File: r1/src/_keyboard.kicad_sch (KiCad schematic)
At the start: 36 parts, among them SW1 REV_TACT, SW10 REV_TACT, SW11 REV_TACT, SW12 REV_TACT, SW13 REV_TACT, SW14 REV_TACT, SW15 REV_TACT, SW16 REV_TACT, SW17 REV_TACT, SW18 REV_TACT, SW19 REV_TACT, SW2 REV_TACT, SW20 REV_TACT, SW21 REV_TACT, SW22 REV_TACT, SW23 REV_TACT, SW24 REV_TACT, SW25 REV_TACT, SW26 REV_TACT, SW27 REV_TACT, SW28 REV_TACT, SW29 REV_TACT, SW3 REV_TACT, SW30 REV_TACT, SW31 REV_TACT, SW32 REV_TACT, SW4 REV_TACT, SW5 REV_TACT, SW6 REV_TACT, SW7 REV_TACT, SW8 REV_TACT, SW9 REV_TACT, U10 PCA9555, U6 PCA9555

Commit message: Assign MPN's and LCSC part numbers
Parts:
- U10, U6: value PCA9555 -> PCA9555PW; LCSC (none) -> C128392; MPN (none) -> PCA9555PW
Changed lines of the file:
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@@
       (effects (font (size 1.27 1.27)) (justify left))
     )
-    (property "Value" "PCA9555" (at 74.3459 114.3 0)
+    (property "Value" "PCA9555PW" (at 74.3459 114.3 0)
       (effects (font (size 1.27 1.27)) (justify left))
     )
@@
     )
     (property "Datasheet" "" (at 72.39 137.16 0)
+      (effects (font (size 1.27 1.27)) hide)
+    )
+    (property "MPN" "PCA9555PW" (at 72.39 137.16 0)
+      (effects (font (size 1.27 1.27)) hide)
+    )
+    (property "LCSC" "C128392" (at 72.39 137.16 0)
       (effects (font (size 1.27 1.27)) hide)
     )
@@
       (effects (font (size 1.27 1.27)) (justify left))
     )
-    (property "Value" "PCA9555" (at 74.3459 40.64 0)
+    (property "Value" "PCA9555PW" (at 74.3459 40.64 0)
       (effects (font (size 1.27 1.27)) (justify left))
     )
@@
       (effects (font (size 1.27 1.27)) hide)
     )
+    (property "MPN" "PCA9555PW" (at 72.39 63.5 0)
+      (effects (font (size 1.27 1.27)) hide)
+    )
+    (property "LCSC" "C128392" (at 72.39 63.5 0)
+      (effects (font (size 1.27 1.27)) hide)
+    )

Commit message: Assign manufacturers
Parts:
- U10, U6: Manufacturer (none) -> Texas Instruments
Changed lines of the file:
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@@
+      (effects (font (size 1.27 1.27)) hide)
+    )
+    (property "Manufacturer" "Texas Instruments" (at 72.39 137.16 0)
       (effects (font (size 1.27 1.27)) hide)
     )
@@
       (effects (font (size 1.27 1.27)) hide)
     )
+    (property "Manufacturer" "Texas Instruments" (at 72.39 63.5 0)
+      (effects (font (size 1.27 1.27)) hide)
+    )

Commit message: Reannotate component refs
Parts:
- renumbered SW11 to SW10, SW21 to SW11, SW22 to SW12, SW4 to SW13, SW12 to SW14, SW23 to SW15, SW24 to SW16, SW5 to SW17, SW13 to SW18, SW25 to SW19, SW9 to SW2, SW26 to SW20, SW6 to SW21, SW14 to SW22, SW27 to SW23, SW28 to SW24, SW7 to SW25, SW15 to SW26, SW29 to SW27, SW30 to SW28, SW8 to SW29, SW17 to SW3, SW16 to SW30, SW18 to SW4, SW2 to SW5, SW10 to SW6, SW19 to SW7, SW20 to SW8, SW3 to SW9, U6 to U7, U10 to U8

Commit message: Assign footprints from jeffmakes-footprints lib
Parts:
- SW1: footprint (none) -> jeffmakes_footprints:microSD_HC_Sofng_TF-15
- U7: footprint (none) -> jeffmakes_footprints:SW_JS1400BFQ-arrows
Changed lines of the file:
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@@
       (effects (font (size 1.27 1.27)) (justify left))
     )
-    (property "Footprint" "" (at 72.39 63.5 0)
+    (property "Footprint" "jeffmakes_footprints:SW_JS1400BFQ-arrows" (at 72.39 63.5 0)
       (effects (font (size 1.27 1.27)) hide)
     )
@@
       (effects (font (size 1.27 1.27)) (justify right))
     )
-    (property "Footprint" "" (at 133.35 52.07 0)
-      (effects (font (size 1.27 1.27)) hide)
-    )
+    (property "Footprint" "jeffmakes_footprints:microSD_HC_Sofng_TF-15" (at 133.35 52.07 0)
+      (effects (font (size 1.27 1.27)) hide)
+    )

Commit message: Assign footprints
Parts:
- SW1: footprint jeffmakes_footprints:microSD_HC_Sofng_TF-15 -> (none)
- U7: footprint jeffmakes_footprints:SW_JS1400BFQ-arrows -> Package_SO:TSSOP-24_4.4x7.8mm_P0.65mm
- U8: footprint (none) -> Package_SO:TSSOP-24_4.4x7.8mm_P0.65mm
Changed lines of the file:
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@@
       (effects (font (size 1.27 1.27)) (justify left))
     )
-    (property "Footprint" "" (at 72.39 137.16 0)
+    (property "Footprint" "Package_SO:TSSOP-24_4.4x7.8mm_P0.65mm" (at 72.39 137.16 0)
       (effects (font (size 1.27 1.27)) hide)
     )
@@
       (effects (font (size 1.27 1.27)) (justify left))
     )
-    (property "Footprint" "jeffmakes_footprints:SW_JS1400BFQ-arrows" (at 72.39 63.5 0)
+    (property "Footprint" "Package_SO:TSSOP-24_4.4x7.8mm_P0.65mm" (at 72.39 63.5 0)
       (effects (font (size 1.27 1.27)) hide)
     )
@@
       (effects (font (size 1.27 1.27)) (justify right))
     )
-    (property "Footprint" "jeffmakes_footprints:microSD_HC_Sofng_TF-15" (at 133.35 52.07 0)
-      (effects (font (size 1.27 1.27)) hide)
-    )
+    (property "Footprint" "" (at 133.35 52.07 0)
+      (effects (font (size 1.27 1.27)) hide)
+    )

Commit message: Assign footprints
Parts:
- SW1, SW10, SW11, SW12, SW13, SW14, SW15, SW16, SW17, SW18, SW19, SW2, SW20, SW21, SW22, SW23, SW24, SW25, SW26, SW27, SW28, SW29, SW3, SW30, SW31, SW32, SW4, SW5, SW6, SW7, SW8, SW9: footprint (none) -> jeffmakes_footprints:SW_SPST_TACT_6x6_REV_MOUNT
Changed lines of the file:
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@@
       (effects (font (size 1.27 1.27)) (justify right))
     )
-    (property "Footprint" "" (at 240.03 77.47 0)
+    (property "Footprint" "jeffmakes_footprints:SW_SPST_TACT_6x6_REV_MOUNT" (at 240.03 77.47 0)
       (effects (font (size 1.27 1.27)) hide)
     )
@@
       (effects (font (size 1.27 1.27)) (justify right))
     )
-    (property "Footprint" "" (at 163.83 128.27 0)
+    (property "Footprint" "jeffmakes_footprints:SW_SPST_TACT_6x6_REV_MOUNT" (at 163.83 128.27 0)
       (effects (font (size 1.27 1.27)) hide)
     )
@@
       (effects (font (size 1.27 1.27)) (justify right))
     )
-    (property "Footprint" "" (at 194.31 128.27 0)
+    (property "Footprint" "jeffmakes_footprints:SW_SPST_TACT_6x6_REV_MOUNT" (at 194.31 128.27 0)
       (effects (font (size 1.27 1.27)) hide)
     )
@@
       (effects (font (size 1.27 1.27)) (justify right))
     )
-    (property "Footprint" "" (at 133.35 102.87 0)
+    (property "Footprint" "jeffmakes_footprints:SW_SPST_TACT_6x6_REV_MOUNT" (at 133.35 102.87 0)
       (effects (font (size 1.27 1.27)) hide)
     )
@@
       (effects (font (size 1.27 1.27)) (justify right))
     )
-    (property "Footprint" "" (at 224.79 102.87 0)
+    (property "Footprint" "jeffmakes_footprints:SW_SPST_TACT_6x6_REV_MOUNT" (at 224.79 102.87 0)
       (effects (font (size 1.27 1.27)) hide)
     )
@@
       (effects (font (size 1.27 1.27)) (justify right))
     )
-    (property "Footprint" "" (at 240.03 128.27 0)
+    (property "Footprint" "jeffmakes_footprints:SW_SPST_TACT_6x6_REV_MOUNT" (at 240.03 128.27 0)
       (effects (font (size 1.27 1.27)) hide)
     )
@@
       (effects (font (size 1.27 1.27)) (justify right))
     )
-    (property "Footprint" "" (at 179.07 77.47 0)
+    (property "Footprint" "jeffmakes_footprints:SW_SPST_TACT_6x6_REV_MOUNT" (at 179.07 77.47 0)
       (effects (font (size 1.27 1.27)) hide)
     )
@@
       (effects (font (size 1.27 1.27)) (justify right))
     )
-    (property "Footprint" "" (at 179.07 52.07 0)
+    (property "Footprint" "jeffmakes_footprints:SW_SPST_TACT_6x6_REV_MOUNT" (at 179.07 52.07 0)
       (effects (font (size 1.27 1.27)) hide)
     )
@@
       (effects (font (size 1.27 1.27)) (justify right))
     )
-    (property "Footprint" "" (at 209.55 102.87 0)
+    (property "Footprint" "jeffmakes_footprints:SW_SPST_TACT_6x6_REV_MOUNT" (at 209.55 102.87 0)
       (effects (font (size 1.27 1.27)) hide)
     )
@@
       (effects (font (size 1.27 1.27)) (justify right))
     )
-    (property "Footprint" "" (at 209.55 77.47 0)
+    (property "Footprint" "jeffmakes_footprints:SW_SPST_TACT_6x6_REV_MOUNT" (at 209.55 77.47 0)
       (effects (font (size 1.27 1.27)) hide)
     )
@@
       (effects (font (size 1.27 1.27)) (justify right))
     )
-    (property "Footprint" "" (at 179.07 102.87 0)
+    (property "Footprint" "jeffmakes_footprints:SW_SPST_TACT_6x6_REV_MOUNT" (at 179.07 102.87 0)
       (effects (font (size 1.27 1.27)) hide)
     )
@@
       (effects (font (size 1.27 1.27)) (justify right))
     )
-    (property "Footprint" "" (at 240.03 52.07 0)
+    (property "Footprint" "jeffmakes_footprints:SW_SPST_TACT_6x6_REV_MOUNT" (at 240.03 52.07 0)
       (effects (font (size 1.27 1.27)) hide)
     )
@@
       (effects (font (size 1.27 1.27)) (justify right))
     )
-    (property "Footprint" "" (at 148.59 77.47 0)
+    (property "Footprint" "jeffmakes_footprints:SW_SPST_TACT_6x6_REV_MOUNT" (at 148.59 77.47 0)
       (effects (font (size 1.27 1.27)) hide)
     )
@@
       (effects (font (size 1.27 1.27)) (justify right))
     )
-    (property "Footprint" "" (at 240.03 102.87 0)
+    (property "Footprint" "jeffmakes_footprints:SW_SPST_TACT_6x6_REV_MOUNT" (at 240.03 102.87 0)
       (effects (font (size 1.27 1.27)) hide)
     )
@@
       (effects (font (size 1.27 1.27)) (justify right))
     )
-    (property "Footprint" "" (at 209.55 128.27 0)
+    (property "Footprint" "jeffmakes_footprints:SW_SPST_TACT_6x6_REV_MOUNT" (at 209.55 128.27 0)
       (effects (font (size 1.27 1.27)) hide)
     )
@@
       (effects (font (size 1.27 1.27)) (justify right))
     )
-    (property "Footprint" "" (at 133.35 77.47 0)
+    (property "Footprint" "jeffmakes_footprints:SW_SPST_TACT_6x6_REV_MOUNT" (at 133.35 77.47 0)
       (effects (font (size 1.27 1.27)) hide)
     )
@@
       (effects (font (size 1.27 1.27)) (justify right))
     )
-    (property "Footprint" "" (at 224.79 77.47 0)
+    (property "Footprint" "jeffmakes_footprints:SW_SPST_TACT_6x6_REV_MOUNT" (at 224.79 77.47 0)
       (effects (font (size 1.27 1.27)) hide)
     )
@@
       (effects (font (size 1.27 1.27)) (justify right))
     )
-    (property "Footprint" "" (at 148.59 52.07 0)
+    (property "Footprint" "jeffmakes_footprints:SW_SPST_TACT_6x6_REV_MOUNT" (at 148.59 52.07 0)
       (effects (font (size 1.27 1.27)) hide)
     )
@@
       (effects (font (size 1.27 1.27)) (justify right))
     )
-    (property "Footprint" "" (at 133.35 52.07 0)
+    (property "Footprint" "jeffmakes_footprints:SW_SPST_TACT_6x6_REV_MOUNT" (at 133.35 52.07 0)
       (effects (font (size 1.27 1.27)) hide)
     )
@@
       (effects (font (size 1.27 1.27)) (justify right))
     )
-    (property "Footprint" "" (at 163.83 77.47 0)
+    (property "Footprint" "jeffmakes_footprints:SW_SPST_TACT_6x6_REV_MOUNT" (at 163.83 77.47 0)
       (effects (font (size 1.27 1.27)) hide)
     )
@@
       (effects (font (size 1.27 1.27)) (justify right))
     )
-    (property "Footprint" "" (at 224.79 128.27 0)
+    (property "Footprint" "jeffmakes_footprints:SW_SPST_TACT_6x6_REV_MOUNT" (at 224.79 128.27 0)
       (effects (font (size 1.27 1.27)) hide)
     )
@@
       (effects (font (size 1.27 1.27)) (justify right))
     )
-    (property "Footprint" "" (at 179.07 128.27 0)
+    (property "Footprint" "jeffmakes_footprints:SW_SPST_TACT_6x6_REV_MOUNT" (at 179.07 128.27 0)
       (effects (font (size 1.27 1.27)) hide)
     )
@@
       (effects (font (size 1.27 1.27)) (justify right))
     )
-    (property "Footprint" "" (at 163.83 102.87 0)
+    (property "Footprint" "jeffmakes_footprints:SW_SPST_TACT_6x6_REV_MOUNT" (at 163.83 102.87 0)
       (effects (font (size 1.27 1.27)) hide)
     )
@@
       (effects (font (size 1.27 1.27)) (justify right))
     )
-    (property "Footprint" "" (at 133.35 128.27 0)
+    (property "Footprint" "jeffmakes_footprints:SW_SPST_TACT_6x6_REV_MOUNT" (at 133.35 128.27 0)
       (effects (font (size 1.27 1.27)) hide)
     )
@@
       (effects (font (size 1.27 1.27)) (justify right))
     )
-    (property "Footprint" "" (at 209.55 52.07 0)
+    (property "Footprint" "jeffmakes_footprints:SW_SPST_TACT_6x6_REV_MOUNT" (at 209.55 52.07 0)
       (effects (font (size 1.27 1.27)) hide)
     )
@@
       (effects (font (size 1.27 1.27)) (justify right))
     )
-    (property "Footprint" "" (at 148.59 102.87 0)
+    (property "Footprint" "jeffmakes_footprints:SW_SPST_TACT_6x6_REV_MOUNT" (at 148.59 102.87 0)
       (effects (font (size 1.27 1.27)) hide)
     )
@@
       (effects (font (size 1.27 1.27)) (justify right))
     )
-    (property "Footprint" "" (at 194.31 52.07 0)
+    (property "Footprint" "jeffmakes_footprints:SW_SPST_TACT_6x6_REV_MOUNT" (at 194.31 52.07 0)
       (effects (font (size 1.27 1.27)) hide)
     )
@@
       (effects (font (size 1.27 1.27)) (justify right))
     )
-    (property "Footprint" "" (at 148.59 128.27 0)
+    (property "Footprint" "jeffmakes_footprints:SW_SPST_TACT_6x6_REV_MOUNT" (at 148.59 128.27 0)
       (effects (font (size 1.27 1.27)) hide)
     )
@@
       (effects (font (size 1.27 1.27)) (justify right))
     )
-    (property "Footprint" "" (at 224.79 52.07 0)
+    (property "Footprint" "jeffmakes_footprints:SW_SPST_TACT_6x6_REV_MOUNT" (at 224.79 52.07 0)
       (effects (font (size 1.27 1.27)) hide)
     )
@@
       (effects (font (size 1.27 1.27)) (justify right))
     )
-    (property "Footprint" "" (at 194.31 77.47 0)
+    (property "Footprint" "jeffmakes_footprints:SW_SPST_TACT_6x6_REV_MOUNT" (at 194.31 77.47 0)
       (effects (font (size 1.27 1.27)) hide)
     )
@@
       (effects (font (size 1.27 1.27)) (justify right))
     )
-    (property "Footprint" "" (at 163.83 52.07 0)
+    (property "Footprint" "jeffmakes_footprints:SW_SPST_TACT_6x6_REV_MOUNT" (at 163.83 52.07 0)
       (effects (font (size 1.27 1.27)) hide)
     )
@@
       (effects (font (size 1.27 1.27)) (justify right))
     )
-    (property "Footprint" "" (at 194.31 102.87 0)
-      (effects (font (size 1.27 1.27)) hide)
-    )
+    (property "Footprint" "jeffmakes_footprints:SW_SPST_TACT_6x6_REV_MOUNT" (at 194.31 102.87 0)
+      (effects (font (size 1.27 1.27)) hide)
+    )

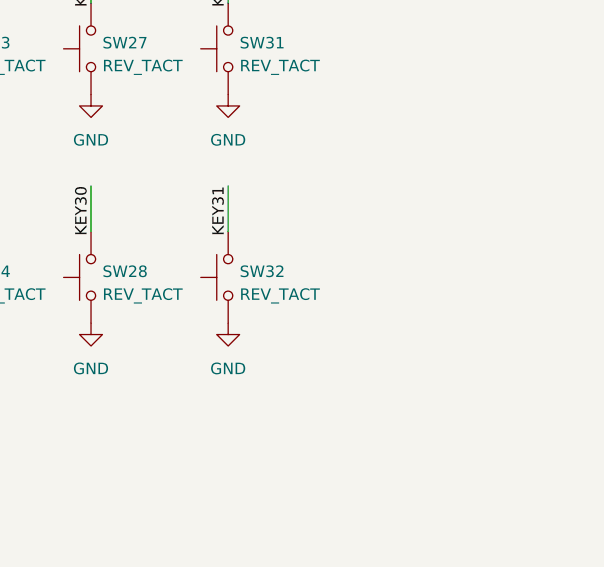
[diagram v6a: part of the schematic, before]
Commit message: ERC pass. Schematic complete.
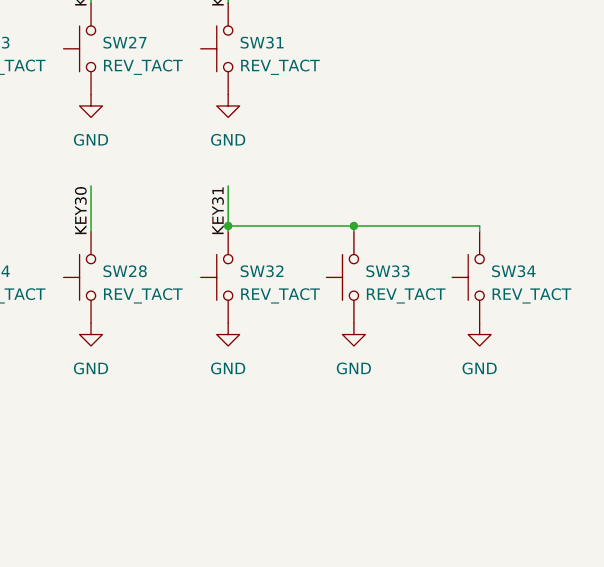
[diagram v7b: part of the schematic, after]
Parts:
- added SW33, SW34: REV_TACT, jeffmakes-footprints:SW_SPST_TACT_6x6_REV_MOUNT, symbol Switch:SW_MEC_5G
- SW1, SW10, SW11, SW12, SW13, SW14, SW15, SW16, SW17, SW18, SW19, SW2, SW20, SW21, SW22, SW23, SW24, SW25, SW26, SW27, SW28, SW29, SW3, SW30, SW31, SW32, SW4, SW5, SW6, SW7, SW8, SW9: footprint jeffmakes_footprints:SW_SPST_TACT_6x6_REV_MOUNT -> jeffmakes-footprints:SW_SPST_TACT_6x6_REV_MOUNT
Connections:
- net GND: now also SW33.1 (A), SW33.2 (A), SW34.1 (A), SW34.2 (A)
- net KEY31: now also SW33.3 (B), SW33.4 (B), SW34.3 (B), SW34.4 (B)

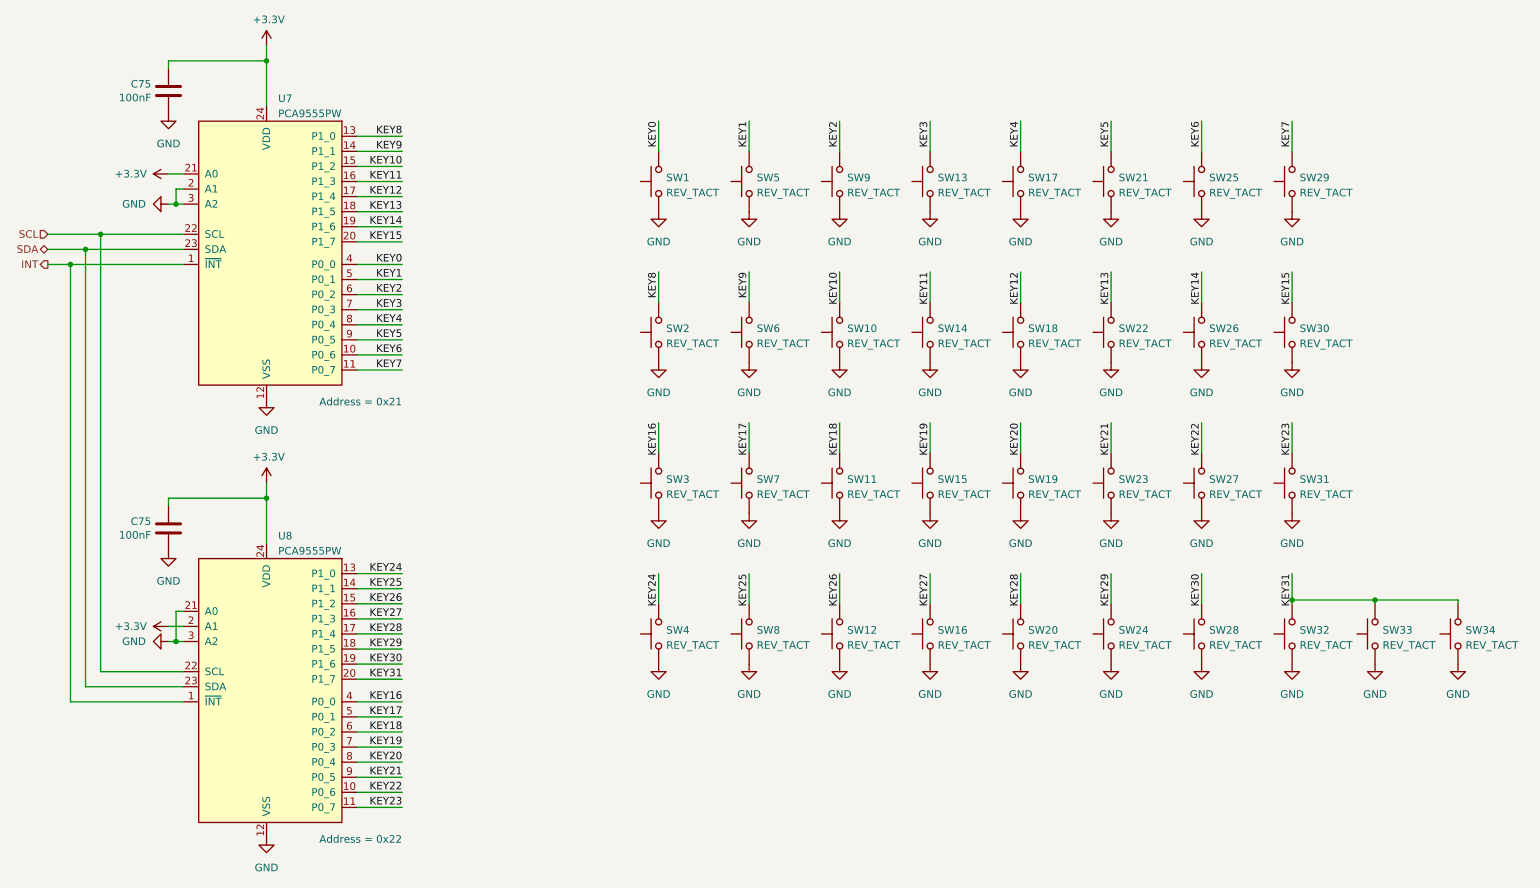
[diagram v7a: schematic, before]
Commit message: Remove duplicate connections from keyboard switches
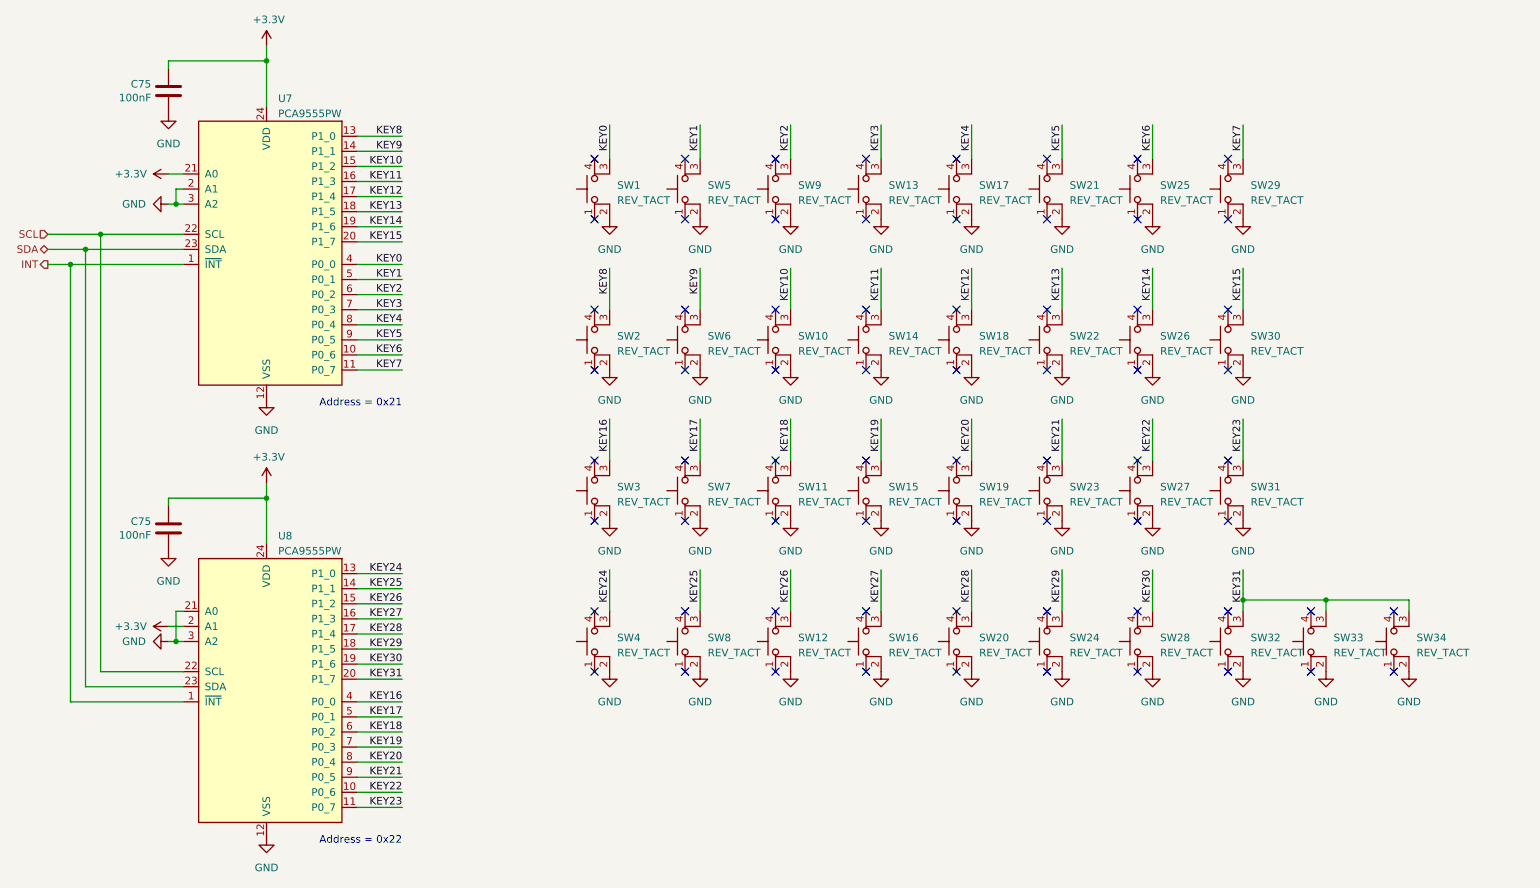
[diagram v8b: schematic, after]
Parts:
- SW1, SW10, SW11, SW12, SW13, SW14, SW15, SW16, SW17, SW18, SW19, SW2, SW20, SW21, SW22, SW23, SW24, SW25, SW26, SW27, SW28, SW29, SW3, SW30, SW31, SW32, SW33, SW34, SW4, SW5, SW6, SW7, SW8, SW9: symbol Switch:SW_MEC_5G -> Switch:SW_MEC_5E
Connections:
- net GND: no longer SW1.1 (A), SW10.1 (A), SW11.1 (A), SW12.1 (A), SW13.1 (A), SW14.1 (A), SW15.1 (A), SW16.1 (A), SW17.1 (A), SW18.1 (A), SW19.1 (A), SW2.1 (A), SW20.1 (A), SW21.1 (A), SW22.1 (A), SW23.1 (A), SW24.1 (A), SW25.1 (A), SW26.1 (A), SW27.1 (A), SW28.1 (A), SW29.1 (A), SW3.1 (A), SW30.1 (A), SW31.1 (A), SW32.1 (A), SW33.1 (A), SW34.1 (A), SW4.1 (A), SW5.1 (A), SW6.1 (A), SW7.1 (A), SW8.1 (A), SW9.1 (A)
- net KEY0: no longer SW1.4 (B)
- net KEY1: no longer SW5.4 (B)
- net KEY10: no longer SW10.4 (B)
- net KEY11: no longer SW14.4 (B)
- net KEY12: no longer SW18.4 (B)
- net KEY13: no longer SW22.4 (B)
- net KEY14: no longer SW26.4 (B)
- net KEY15: no longer SW30.4 (B)
- net KEY16: no longer SW3.4 (B)
- net KEY17: no longer SW7.4 (B)
- net KEY18: no longer SW11.4 (B)
- net KEY19: no longer SW15.4 (B)
- net KEY2: no longer SW9.4 (B)
- net KEY20: no longer SW19.4 (B)
- net KEY21: no longer SW23.4 (B)
- net KEY22: no longer SW27.4 (B)
- net KEY23: no longer SW31.4 (B)
- net KEY24: no longer SW4.4 (B)
- net KEY25: no longer SW8.4 (B)
- net KEY26: no longer SW12.4 (B)
- net KEY27: no longer SW16.4 (B)
- net KEY28: no longer SW20.4 (B)
- net KEY29: no longer SW24.4 (B)
- net KEY3: no longer SW13.4 (B)
- net KEY30: no longer SW28.4 (B)
- net KEY31: no longer SW32.4 (B), SW33.4 (B), SW34.4 (B)
- net KEY4: no longer SW17.4 (B)
- net KEY5: no longer SW21.4 (B)
- net KEY6: no longer SW25.4 (B)
- net KEY7: no longer SW29.4 (B)
- net KEY8: no longer SW2.4 (B)
- net KEY9: no longer SW6.4 (B)
- no-connect marks 0 -> 68
